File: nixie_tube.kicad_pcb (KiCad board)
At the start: 2 copper layers, 25.8 x 56.3 mm, 28 parts, among them J1 Conn_01x06_Male, J11 dc003a, J2 Conn_01x06_Female, J3 Conn_01x01_Male, J4 Conn_01x01_Female, Q1 SS8550, Q2 FQD5N60C, Q3 MMBTA42LT1, Q4 AO3407, U1 MC34063

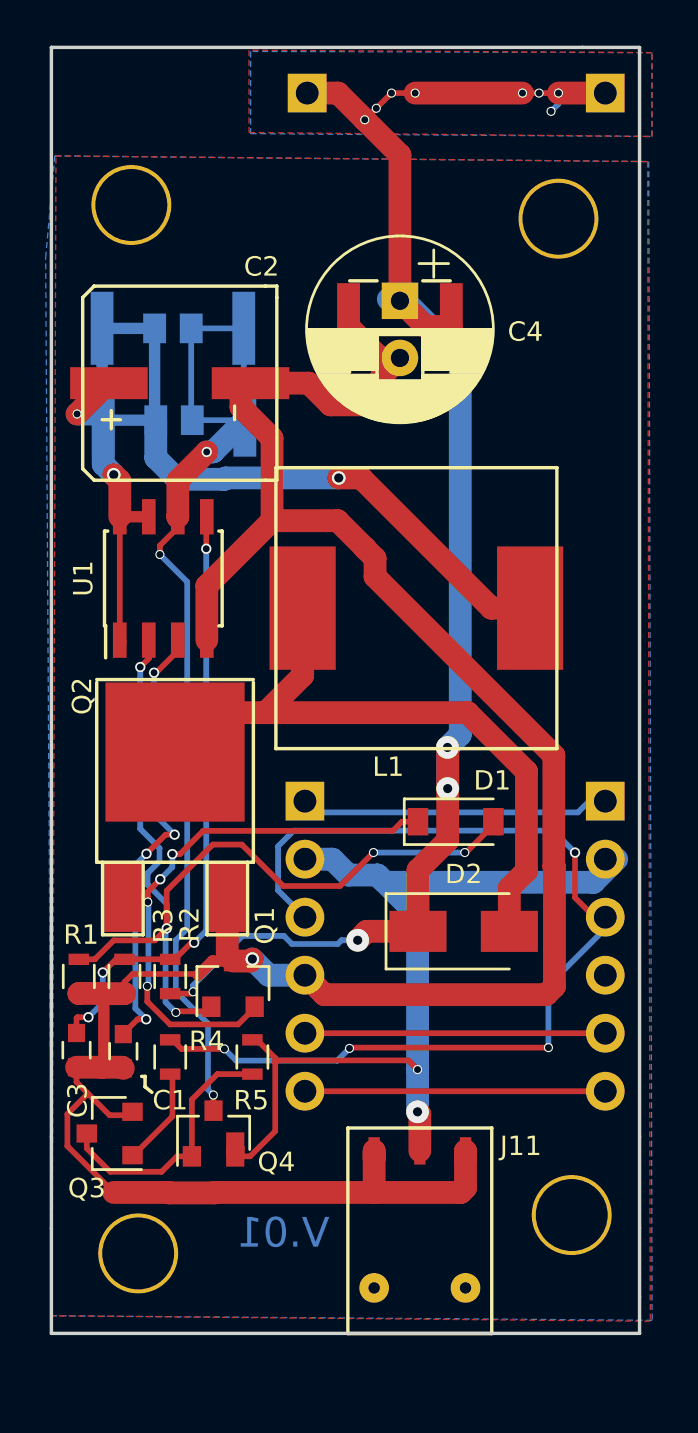
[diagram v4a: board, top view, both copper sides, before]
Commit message: added panelizer folder project and panelized result
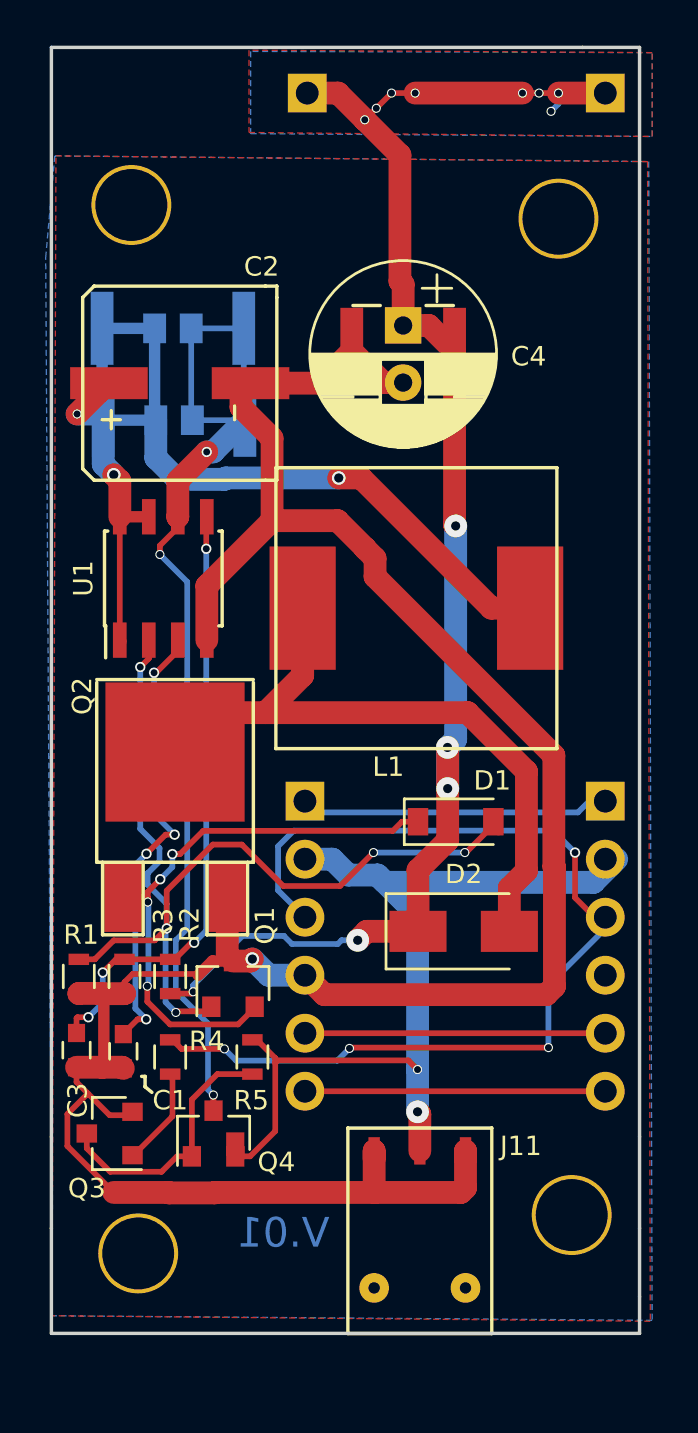
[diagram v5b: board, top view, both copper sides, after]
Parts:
- moved C4 1.09 mm to (181.9, 93.1)
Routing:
- net GND: track 111.7 -> 108.5 mm
- net Net-(C4-Pad1): track 70.6 -> 67.7 mm, vias 12 -> 13
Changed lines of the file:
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@@
     (links 56)
     (no_connects 0)
-    (area 156.600001 78.6585 202.925239 141.300001)
+    (area 156.600001 79.724999 202.925239 141.300001)
     (thickness 1.6)
     (drawings 24)
-    (tracks 355)
+    (tracks 354)
     (zones 0)
     (modules 28)
@@
     (visible_elements 7FFEDFFF)
     (pcbplotparams
-      (layerselection 0x310fc_80000001)
+      (layerselection 0x010fc_80000001)
       (usegerberextensions true)
       (usegerberattributes true)
@@
   )
   (module nixie-tube-fp:CP_RADIAL_and_mlcc (layer F.Cu)
-    (at 181.76 92.02 270)
+    (at 181.9 93.1 270)
     (descr "CP, Radial series, Radial, pin pitch=2.50mm, , diameter=8mm, Electrolytic Capacitor")
     (tags "CP Radial series Radial pin pitch 2.50mm  diameter 8mm Electrolytic Capacitor")
@@
   (segment (start 172.035 105.75) (end 172.035 106.225) (width 0.25) (layer F.Cu) (net 1) (status 30))
   (via (at 170.995547 107.175488) (size 0.453) (drill 0.3) (layers F.Cu B.Cu) (net 1))
+  (segment (start 179.65 93.1) (end 181.025 94.475) (width 1) (layer F.Cu) (net 2))
+  (segment (start 181.025 94.475) (end 181.9 94.475) (width 1) (layer F.Cu) (net 2))
+  (segment (start 175.22 94.5) (end 178.25 94.5) (width 1) (layer F.Cu) (net 2))
+  (segment (start 178.25 94.5) (end 179.65 93.1) (width 1) (layer F.Cu) (net 2))
   (segment (start 168.1 125.6) (end 167.2 126.5) (width 0.25) (layer F.Cu) (net 2))
   (segment (start 167.2 126.5) (end 167.2 127.9) (width 0.25) (layer F.Cu) (net 2))
@@
   (segment (start 168.1 125.6) (end 169.05 126.55) (width 0.25) (layer F.Cu) (net 2))
   (segment (start 167.6 125.1) (end 168.1 125.6) (width 0.25) (layer F.Cu) (net 2))
-  (segment (start 167.6 124.45) (end 167.6 125.1) (width 0.25) (layer F.Cu) (net 2))
-  (segment (start 169.05 126.55) (end 169.9 126.55) (width 0.25) (layer F.Cu) (net 2))
-  (segment (start 169.9 126.55) (end 170.05 126.4) (width 0.25) (layer F.Cu) (net 2))
+  (segment (start 167.6 124.45) (end 167.6 125.1) (width 0.25) (layer F.Cu) (net 2) (status 10))
+  (segment (start 169.05 126.55) (end 169.9 126.55) (width 0.25) (layer F.Cu) (net 2) (status 20))
+  (segment (start 169.9 126.55) (end 170.05 126.4) (width 0.25) (layer F.Cu) (net 2) (status 30))
   (segment (start 172.866184 120.366186) (end 172.924999 120.425001) (width 0.25) (layer F.Cu) (net 2))
   (segment (start 169.7 120.725) (end 170.058814 120.366186) (width 0.25) (layer F.Cu) (net 2))
@@
   (segment (start 167.708302 121.216698) (end 168.600171 121.216698) (width 1) (layer F.Cu) (net 2) (status 10))
   (segment (start 169.698498 121.226502) (end 169.7 121.225) (width 1) (layer F.Cu) (net 2) (status 30))
-  (segment (start 181.76 93.395) (end 180.960001 94.194999) (width 1) (layer F.Cu) (net 2) (status 10))
-  (segment (start 180.960001 94.194999) (end 180.960001 94.819999) (width 1) (layer F.Cu) (net 2))
-  (segment (start 180.960001 94.819999) (end 180.33 95.45) (width 1) (layer F.Cu) (net 2))
-  (segment (start 179.51 92.02) (end 180.885 93.395) (width 1) (layer F.Cu) (net 2) (status 10))
-  (segment (start 180.885 93.395) (end 181.76 93.395) (width 1) (layer F.Cu) (net 2) (status 20))
-  (segment (start 175.22 94.5) (end 177.77 94.5) (width 1) (layer F.Cu) (net 2) (status 10))
-  (segment (start 177.77 94.5) (end 178.72 95.45) (width 1) (layer F.Cu) (net 2))
-  (segment (start 178.72 95.45) (end 180.33 95.45) (width 1) (layer F.Cu) (net 2))
   (segment (start 174.45 119.8) (end 175.209114 119.8) (width 1) (layer F.Cu) (net 2) (status 10))
   (segment (start 175.209114 119.8) (end 175.297836 119.711278) (width 1) (layer F.Cu) (net 2))
@@
   (segment (start 167.6 122.95) (end 167.6 122.925) (width 0.25) (layer F.Cu) (net 3) (status 30))
   (segment (start 173.2 100.455) (end 173.305 100.35) (width 0.25) (layer F.Cu) (net 3) (status 30))
+  (segment (start 184.2 100.75) (end 184.2 110.09) (width 1) (layer B.Cu) (net 4))
+  (segment (start 184.2 110.09) (end 183.841464 110.448536) (width 1) (layer B.Cu) (net 4))
+  (segment (start 184.15 93.1) (end 184.15 100.7) (width 1) (layer F.Cu) (net 4))
+  (segment (start 184.15 100.7) (end 184.2 100.75) (width 1) (layer F.Cu) (net 4))
+  (via (at 184.2 100.75) (size 1) (drill 0.4) (layers F.Cu B.Cu) (net 4))
+  (segment (start 181.9 91.975) (end 181.9 90.175) (width 1) (layer F.Cu) (net 4))
+  (segment (start 181.9 90.175) (end 181.76 90.035) (width 1) (layer F.Cu) (net 4))
+  (segment (start 181.76 90.035) (end 181.76 84.51) (width 1) (layer F.Cu) (net 4))
+  (segment (start 181.9 91.975) (end 183.025 91.975) (width 1) (layer F.Cu) (net 4))
+  (segment (start 183.025 91.975) (end 184.15 93.1) (width 1) (layer F.Cu) (net 4))
   (segment (start 182.55 115.817996) (end 182.55 118.5) (width 1) (layer F.Cu) (net 4) (status 20))
   (segment (start 183.85 112.25) (end 183.85 114.517996) (width 1) (layer F.Cu) (net 4))
@@
   (segment (start 181.76 84.51) (end 180.22 82.97) (width 1) (layer F.Cu) (net 4))
   (via (at 180.22 82.97) (size 0.4) (drill 0.3) (layers F.Cu B.Cu) (net 4))
-  (segment (start 181.76 90.895) (end 181.76 84.51) (width 1) (layer F.Cu) (net 4) (status 10))
-  (segment (start 182.885 92.02) (end 181.76 90.895) (width 1) (layer F.Cu) (net 4) (status 20))
-  (segment (start 184.01 92.02) (end 182.885 92.02) (width 1) (layer F.Cu) (net 4) (status 10))
   (via (at 179.91 118.89) (size 1) (drill 0.4) (layers F.Cu B.Cu) (net 4))
   (segment (start 182.55 118.5) (end 180.3 118.5) (width 1) (layer F.Cu) (net 4) (status 10))
   (segment (start 180.3 118.5) (end 179.91 118.89) (width 1) (layer F.Cu) (net 4))
   (segment (start 180.22 82.97) (end 179.05 81.8) (width 1) (layer F.Cu) (net 4))
-  (segment (start 181.25 90.825) (end 181.905 90.825) (width 1) (layer B.Cu) (net 4) (status 30))
-  (segment (start 181.905 90.825) (end 184.4 93.32) (width 1) (layer B.Cu) (net 4) (status 10))
-  (segment (start 184.4 93.32) (end 184.4 109.89) (width 1) (layer B.Cu) (net 4))
-  (segment (start 184.4 109.89) (end 183.841464 110.448536) (width 1) (layer B.Cu) (net 4))
   (segment (start 179.05 81.8) (end 177.7 81.8) (width 1) (layer F.Cu) (net 4) (status 20))
   (segment (start 183.85 110.457072) (end 183.841464 110.448536) (width 1) (layer F.Cu) (net 4))
@@
   (segment (start 168.6 94.5) (end 169.6 94.5) (width 0.5) (layer F.Cu) (net 11) (status 30))
   (segment (start 169.55 105.805) (end 169.495 105.75) (width 0.5) (layer F.Cu) (net 11) (status 30))
-  (segment (start 171.8 126.6) (end 171.8 124.95) (width 0.25) (layer F.Cu) (net 12))
-  (segment (start 170.1 128.3) (end 171.8 126.6) (width 0.25) (layer F.Cu) (net 12))
-  (segment (start 171.8 124.95) (end 171.8 124.75) (width 0.25) (layer F.Cu) (net 12))
-  (segment (start 170.05 128.3) (end 170.1 128.3) (width 0.25) (layer F.Cu) (net 12))
+  (segment (start 171.8 126.6) (end 171.8 124.95) (width 0.25) (layer F.Cu) (net 12) (status 20))
+  (segment (start 170.1 128.3) (end 171.8 126.6) (width 0.25) (layer F.Cu) (net 12) (status 10))
+  (segment (start 171.8 124.95) (end 171.8 124.75) (width 0.25) (layer F.Cu) (net 12) (status 30))
+  (segment (start 170.05 128.3) (end 170.1 128.3) (width 0.25) (layer F.Cu) (net 12) (status 30))
   (segment (start 180.78 116.035134) (end 181.09797 116.353104) (width 1) (layer B.Cu) (net 13))
   (segment (start 181.09797 116.353104) (end 190.236896 116.353104) (width 1) (layer B.Cu) (net 13))
@@
   (segment (start 172.62 92.1) (end 174.92 92.1) (width 0.25) (layer B.Cu) (net 15) (status 30))
   (segment (start 172.67 96.12) (end 174.97 96.12) (width 0.25) (layer B.Cu) (net 15) (status 30))
-  (segment (start 168.05 127.35) (end 168.05 128) (width 0.25) (layer F.Cu) (net 16))
+  (segment (start 168.05 127.35) (end 168.05 128) (width 0.25) (layer F.Cu) (net 16) (status 10))
   (segment (start 168.05 128) (end 169.075001 129.025001) (width 0.25) (layer F.Cu) (net 16))
   (segment (start 169.075001 129.025001) (end 171.324999 129.025001) (width 0.25) (layer F.Cu) (net 16))
   (segment (start 171.324999 129.025001) (end 172 128.35) (width 0.25) (layer F.Cu) (net 16))
-  (segment (start 172 128.35) (end 172.65 128.35) (width 0.25) (layer F.Cu) (net 16))
+  (segment (start 172 128.35) (end 172.65 128.35) (width 0.25) (layer F.Cu) (net 16) (status 20))
   (segment (start 175.3 124.75) (end 173.764998 124.75) (width 0.25) (layer F.Cu) (net 16) (status 10))
   (segment (start 172.65 125.864998) (end 172.65 128.35) (width 0.25) (layer F.Cu) (net 16) (status 20))

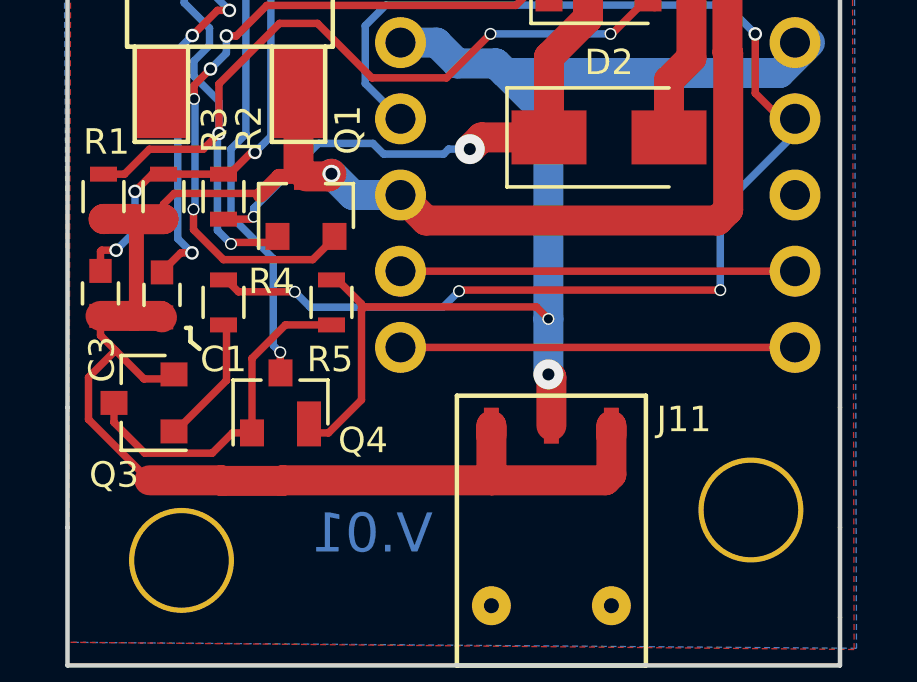
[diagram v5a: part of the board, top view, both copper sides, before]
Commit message: finalized tracks, added skull and lightning symbol
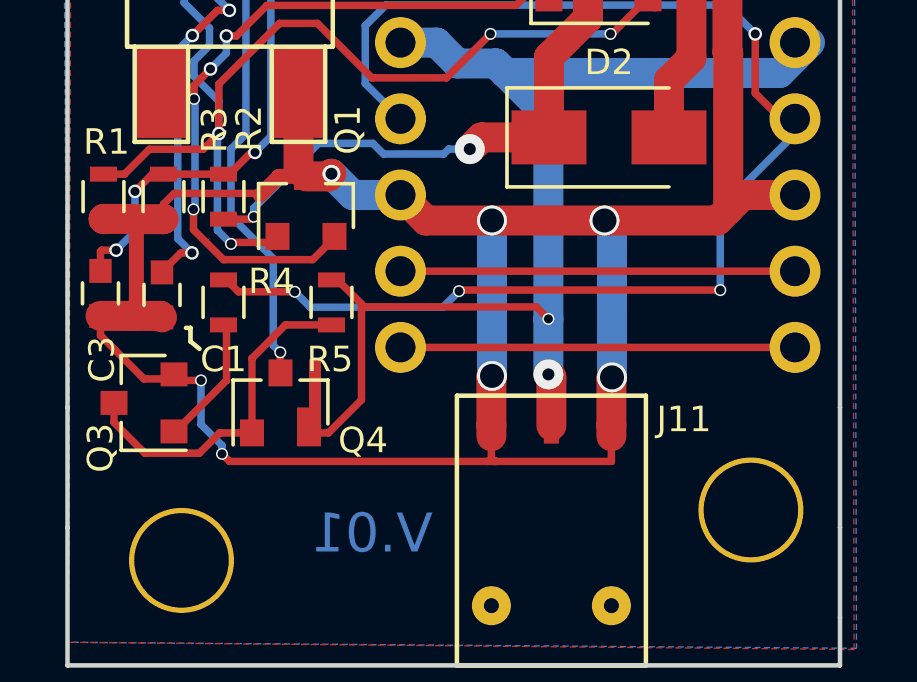
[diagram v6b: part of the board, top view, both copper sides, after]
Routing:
- net GND: track 108.5 -> 119.6 mm, vias 1 -> 7

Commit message: finalized everything and ready to send out
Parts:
- added Z?: lightning, nixie-tube-fp:lightning, B.Cu at (187.3, 82.0)
- added Z?: skull, nixie-tube-fp:skull, B.Cu at (182.1, 82.5)
- added Z?: lightning, nixie-tube-fp:lightning, F.Cu at (187.4, 82.0)
- added Z?: skull, nixie-tube-fp:skull, F.Cu at (182.2, 82.4)
- moved L1 1.12 mm to (183.6, 104.3)
- moved C4 1.12 mm to (181.9, 92.0)
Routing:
- net Net-(C4-Pad1): track 67.7 -> 71.7 mm
- net Net-(D2-Pad2): track 29.7 -> 31.3 mm
- net Net-(C2-Pad1): track 48.8 -> 49.9 mm
